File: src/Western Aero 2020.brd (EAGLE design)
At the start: 122.2 x 139.4 mm, 78 parts, among them IC1 7805DT, IC3 7806DT

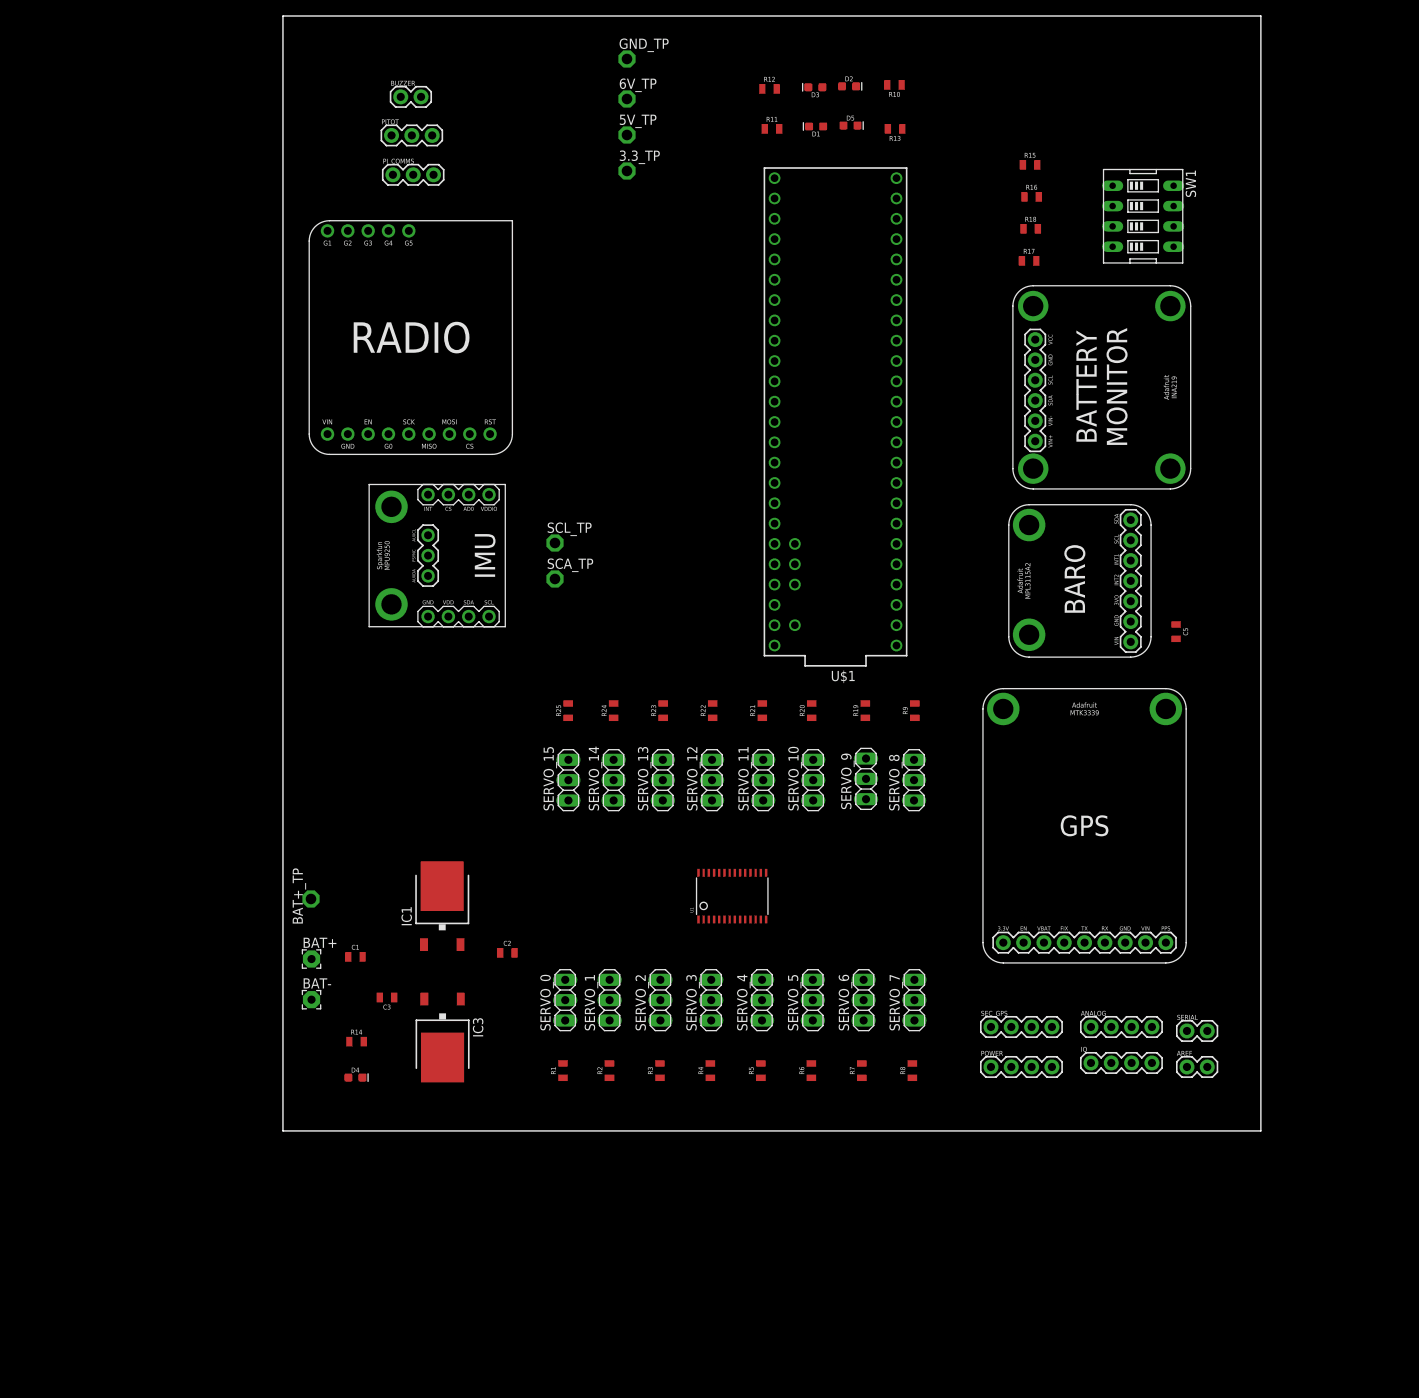
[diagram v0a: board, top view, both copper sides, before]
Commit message: Reconfigured components, hid resistors and cut space
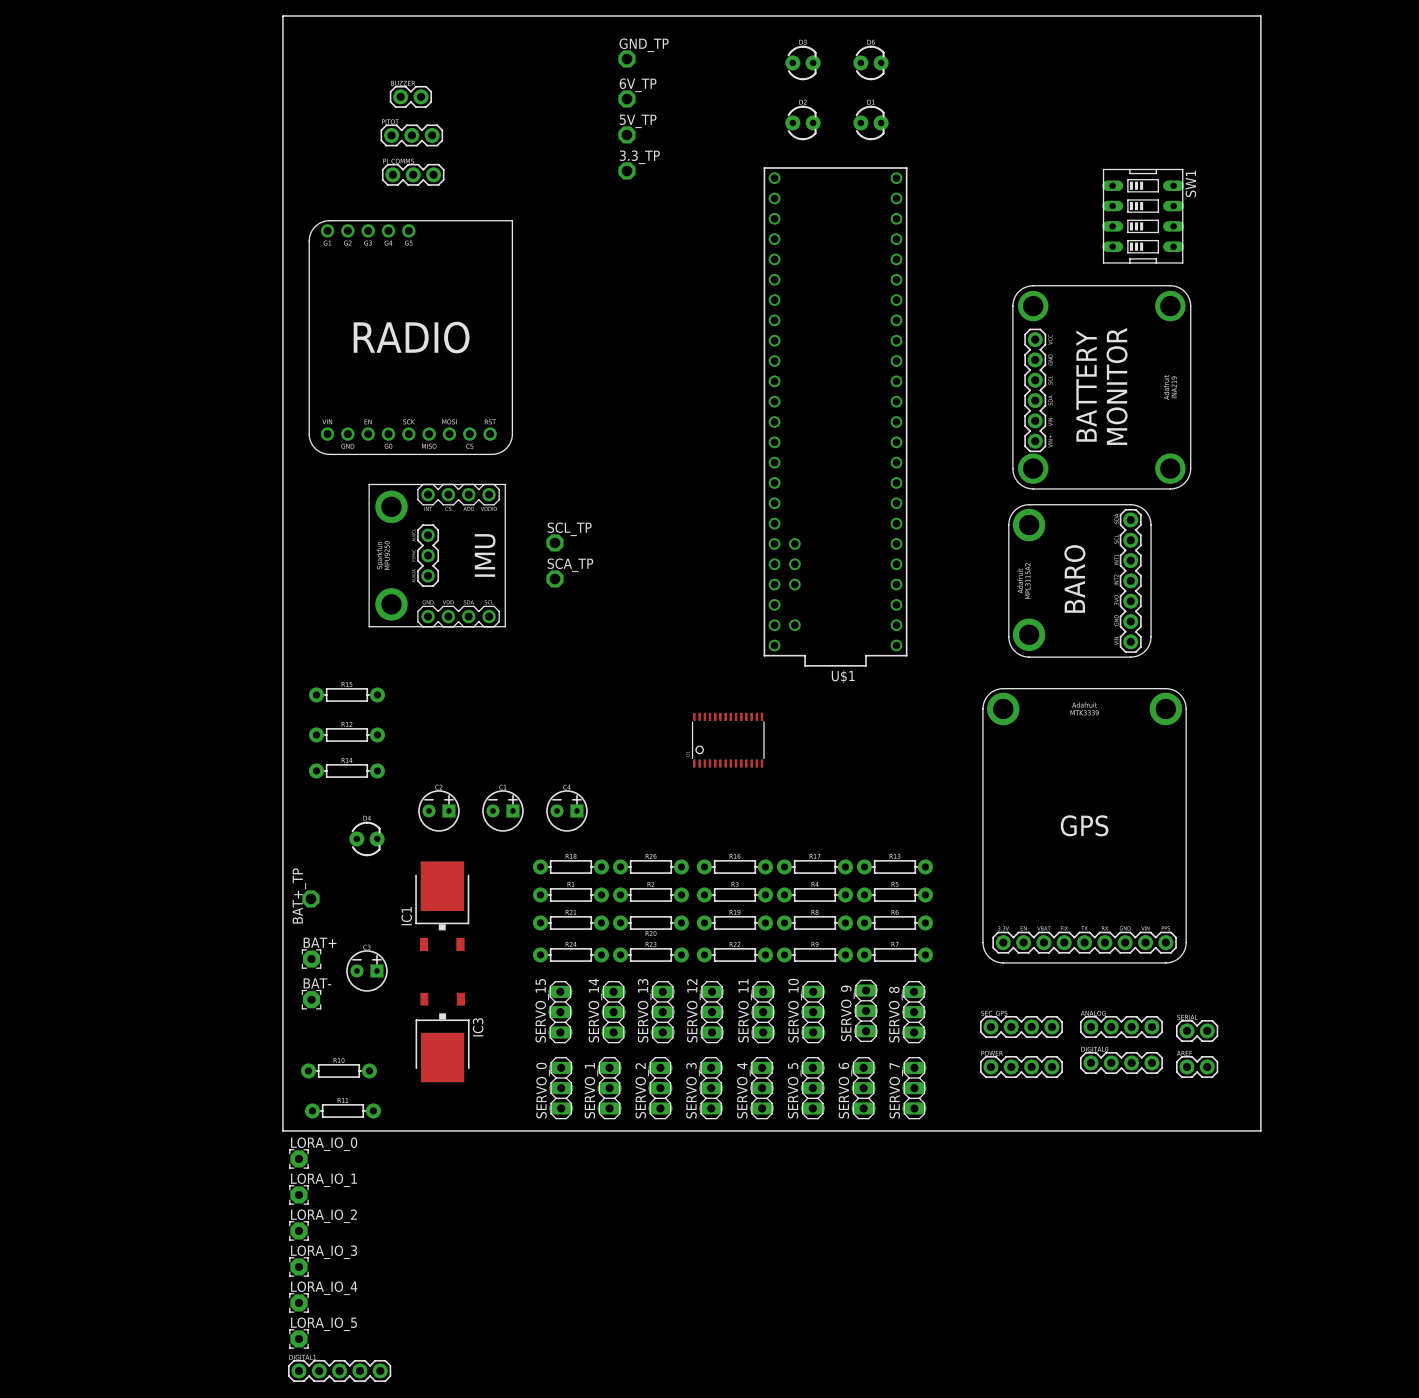
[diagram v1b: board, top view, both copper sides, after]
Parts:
- removed C5: 10µF, SparkFun-Capacitors:0805
- removed D5: WHITE, SparkFun-LED:LED-0603
- removed R25: 220, SparkFun-Resistors:0805
- added C4: 0.1uF, SparkFun-Capacitors:CPOL-RADIAL-2.5MM-5MM
- added D6: Red, SparkFun-LED:LED_3MM
- added DIGITAL1: (no value), SparkFun-Connectors:1X05
- added LORA_IO_0, LORA_IO_1, LORA_IO_2, LORA_IO_3, LORA_IO_4, LORA_IO_5: WIREPAD, wirepad:2,15/1,0
- added R26: 10K, SparkFun-Resistors:AXIAL-0.3
- C1: value 0.33µF -> 10uF; device SparkFun-Capacitors:0805 -> SparkFun-Capacitors:CPOL-RADIAL-2.5MM-5MM
- C2: value 0.1µF -> 0.1uF; device SparkFun-Capacitors:0805 -> SparkFun-Capacitors:CPOL-RADIAL-2.5MM-5MM
- C3: value 0.1µF -> 0.33uF; device SparkFun-Capacitors:0805 -> SparkFun-Capacitors:CPOL-RADIAL-2.5MM-5MM
- D1: value BLUE -> Blue; device SparkFun-LED:LED-0603 -> SparkFun-LED:LED_3MM
- D2: value RED -> Yellow; device SparkFun-LED:LED-0603 -> SparkFun-LED:LED_3MM
- D3: value Yellow -> White; device SparkFun-LED:LED-0603 -> SparkFun-LED:LED_3MM
- D4: value GREEN -> Green; device SparkFun-LED:LED-0603 -> SparkFun-LED:LED_3MM
- R1, R10, R11, R12, R13, R14, R15, R16, R17, R19, R2, R20, R21, R22, R23, R24, R3, R4, R5, R6, R7, R8, R9: device SparkFun-Resistors:0805 -> SparkFun-Resistors:AXIAL-0.3
- R18: value 10K -> 220; device SparkFun-Resistors:0805 -> SparkFun-Resistors:AXIAL-0.3
- moved R10 141.5 mm to (7.00, 7.50), turned to 0 degrees
- moved R11 134.0 mm to (7.50, 2.50)
- moved R15 108.1 mm to (8.00, 54.5)
- moved R18 98.3 mm to (36.0, 33.0)
- moved R12 96.5 mm to (8.00, 49.5)
- moved R13 92.3 mm to (76.5, 33.0), turned to 0 degrees
- moved R16 91.6 mm to (56.5, 33.0)
- moved R17 80.4 mm to (66.5, 33.0)
- moved R21 35.7 mm to (36.0, 26.0), turned to 0 degrees
- moved R14 33.9 mm to (8.00, 45.0)
- moved R20 33.3 mm to (46.0, 26.0), turned to 180 degrees
- moved R9 33.0 mm to (66.5, 22.0), turned to 0 degrees
- moved R19 31.1 mm to (56.5, 26.0), turned to 0 degrees
- moved R24 31.0 mm to (36.0, 22.0), turned to 0 degrees
- moved R22 30.7 mm to (56.5, 22.0), turned to 0 degrees
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- renumbered IO to DIGITAL0
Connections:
- removed net LORA_IO_1: U$1.35/A16, U$3.10
- removed net LORA_IO_2: U$1.36/A17, U$3.11
- removed net LORA_IO_3: U$1.37/A18, U$3.12
- removed net LORA_IO_4: U$1.38/A19, U$3.13
- removed net LORA_IO_5: U$1.39/A20, U$3.14
- new net D35: DIGITAL1.1, U$1.35/A16
- new net D36: DIGITAL1.2, U$1.36/A17
- new net D37: DIGITAL1.3, U$1.37/A18
- new net D38: DIGITAL1.4, U$1.38/A19
- new net D39: DIGITAL1.5, U$1.39/A20
- new net N$10: LORA_IO_2.1, U$3.11
- new net N$25: LORA_IO_4.1, U$3.13
- new net N$26: LORA_IO_3.1, U$3.12
- new net N$27: LORA_IO_0.1, U$3.4
- net 5V: now also C1.1, C4.1; no longer C2.1, C5.2
- net 6V: now also C2.1, SERVO_0.2; no longer C3.1
- net DIP1: now also R26.P$2; no longer R17.2
- net DIP2: now also R15.P$2; no longer R18.2
- net DIP3: now also R16.P$2; no longer R16.2
- net DIP4: now also R17.P$2; no longer R15.2
- net GND: now also C4.2, R10.P$1, R11.P$1, R12.P$1, R13.P$1, R14.P$1, R15.P$1, R16.P$1, R17.P$1, R26.P$1; no longer C5.1, R10.1, R11.1, R12.1, R13.1, R14.1, R15.1, R17.1
- net LORA_INT: no longer U$3.4
- net N$1: now also R18.P$2; no longer R1.2
- net N$11: now also R2.P$2; no longer R3.2
- net N$12: now also R3.P$2; no longer R4.2
- net N$13: now also R4.P$2; no longer R5.2
- net N$14: now also R5.P$2; no longer R6.2
- net N$15: now also R6.P$2; no longer R7.2
- net N$16: now also R7.P$2; no longer R8.2
- net N$17: now also R8.P$2; no longer R9.2
- net N$18: now also R9.P$2; no longer R19.2
- net N$19: now also R19.P$2; no longer R20.2
- net N$2: now also D6.K, R10.P$2; no longer R18.1
- net N$20: now also R20.P$2; no longer R21.2
- net N$21: now also R21.P$2; no longer R22.2
- net N$22: now also R22.P$2; no longer R23.2
- net N$23: now also R23.P$2; no longer R24.2
- net N$24: now also R24.P$2; no longer R25.2
- net N$3: now also D1.K, R11.P$2; no longer D2.C, R10.2
- net N$4: now also D2.K, R12.P$2; no longer R16.1
- net N$5: now also D3.K, R13.P$2; no longer D1.C, R11.2
- net N$6: now also D4.K, R14.P$2; no longer D3.C, R12.2
- net N$7: now also LORA_IO_5.1, U$3.14; no longer D5.C, R13.2
- net N$8: now also LORA_IO_1.1, U$3.10; no longer D4.C, R14.2
- net N$9: now also R1.P$2; no longer R2.2
- net PWM0: now also R18.P$1; no longer R1.1
- net PWM1: now also R1.P$1; no longer R2.1
- net PWM10: now also R19.P$1; no longer R20.1
- net PWM11: now also R20.P$1; no longer R21.1
- net PWM12: now also R21.P$1; no longer R22.1
- net PWM13: now also R22.P$1; no longer R23.1
- net PWM14: now also R23.P$1; no longer R24.1
- net PWM15: now also R24.P$1; no longer R25.1
- net PWM2: now also R2.P$1; no longer R3.1
- net PWM3: now also R3.P$1; no longer R4.1
- net PWM4: now also R4.P$1; no longer R5.1
- net PWM5: now also R5.P$1; no longer R6.1
- net PWM6: now also R6.P$1; no longer R7.1
- net PWM7: now also R7.P$1; no longer R8.1
- net PWM8: now also R8.P$1; no longer R9.1
- net PWM9: now also R9.P$1; no longer R19.1
- net RED_LED: now also D6.A; no longer D2.A
- net VIN-: now also C3.1; no longer C1.1
- net WHITE_LED: now also D3.A; no longer D5.A
- net YELLOW_LED: now also D2.A; no longer D3.A

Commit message: Added screwholes, adjusted addresses, few other tweaks
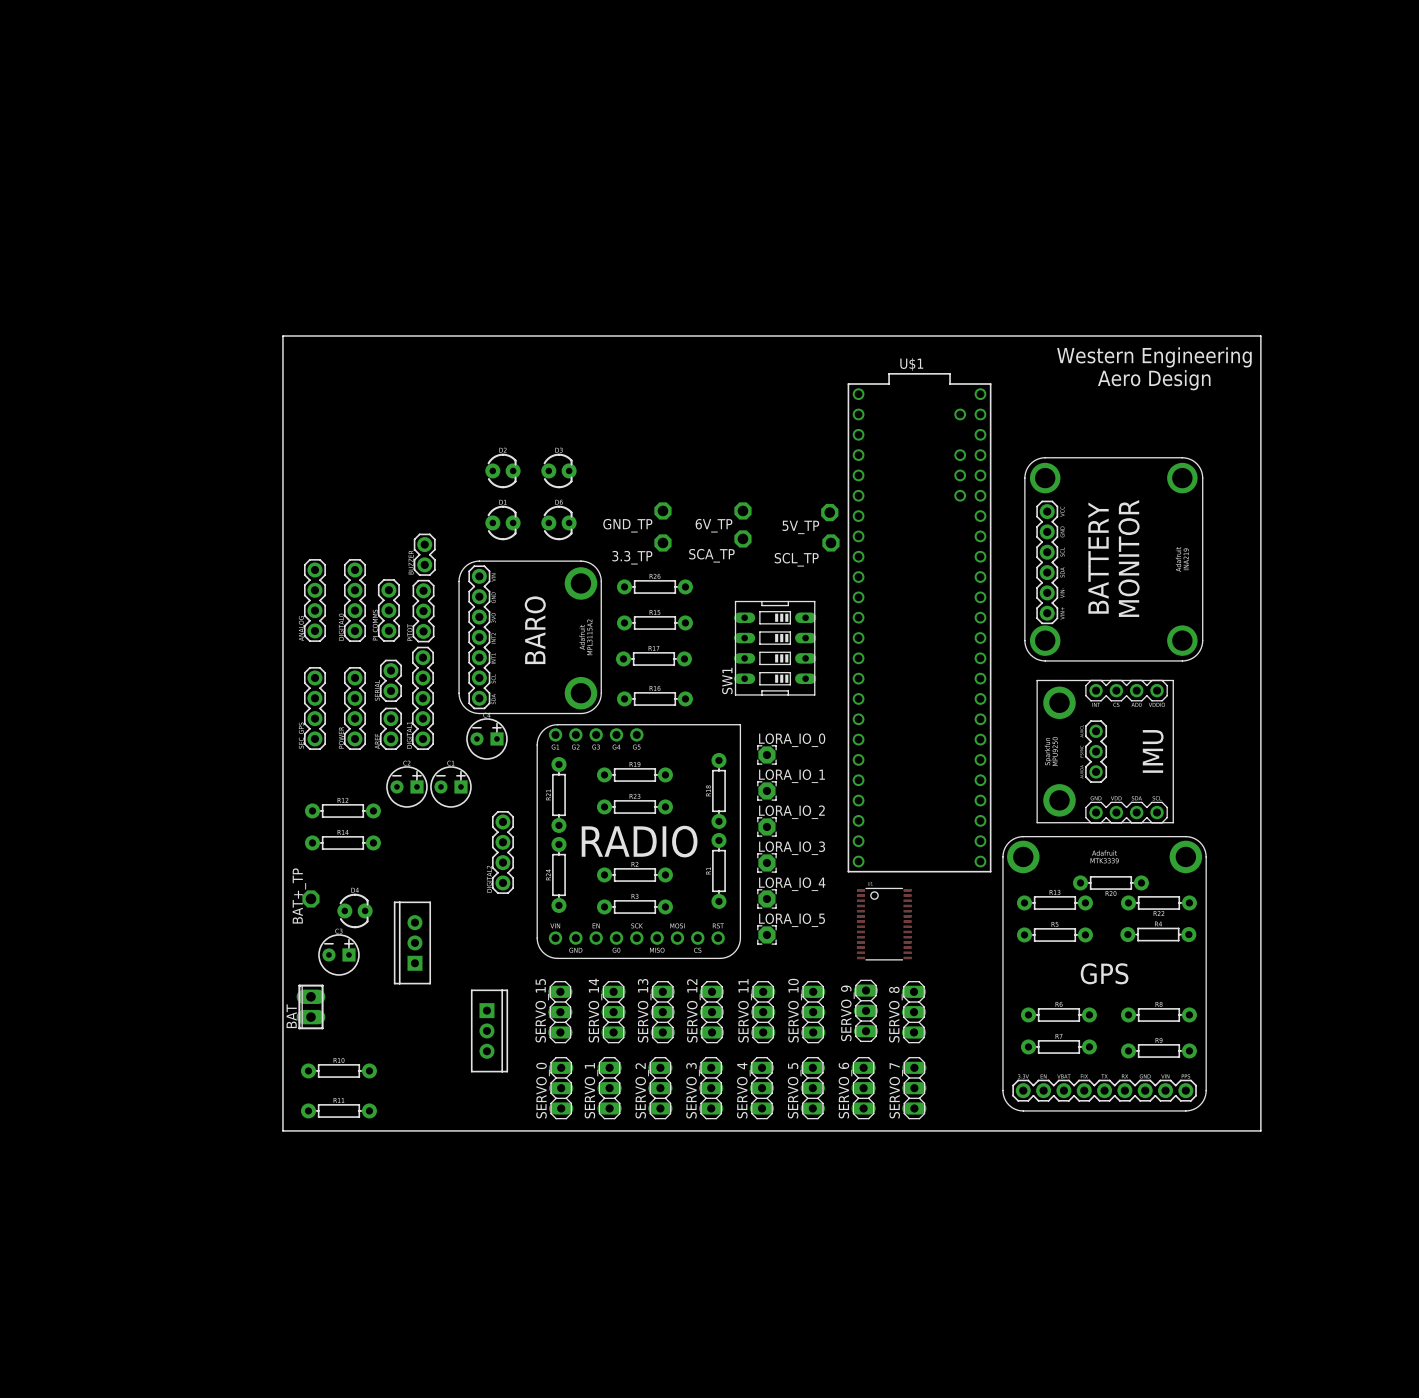
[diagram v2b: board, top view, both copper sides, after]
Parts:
- removed BAT+, BAT-: WIREPAD, wirepad:2,15/1,0
- removed IC1: 7805DT, linear:TO252
- removed IC3: 7806DT, linear:TO252
- added 7805, 7806: (no value), SparkFun-IC-Power:TO220-IGO
- added BAT: (no value), con-phoenix-254:2POL254
- added DIGITAL2: (no value), SparkFun-Connectors:1X04
- moved ANALOG 108.9 mm to (4.00, 62.5), turned to 90 degrees
- moved SERIAL 108.2 mm to (13.5, 55.0), turned to 90 degrees
- moved AREF 107.6 mm to (13.5, 49.0), turned to 90 degrees
- moved DIGITAL0 106.7 mm to (9.00, 62.5), turned to 90 degrees
- moved SEC_GPS 91.8 mm to (4.00, 49.0), turned to 90 degrees
- moved POWER 89.4 mm to (9.00, 49.0), turned to 90 degrees
- moved U$4 87.3 mm to (22.0, 71.2), turned to 270 degrees
- moved U$2 87.0 mm to (111.3, 56.3)
- moved DIGITAL1 80.5 mm to (17.5, 49.0), turned to 90 degrees
- moved LORA_IO_0 77.3 mm to (60.5, 47.0)
- moved LORA_IO_1 77.3 mm to (60.5, 42.5)
- moved LORA_IO_2 77.3 mm to (60.5, 38.0)
- moved LORA_IO_3 77.3 mm to (60.5, 33.5)
- moved LORA_IO_4 77.3 mm to (60.5, 29.0)
- moved LORA_IO_5 77.3 mm to (60.5, 24.5)
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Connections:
- removed net LORA_CS: U$1.33/A14, U$3.8
- new net CS: DIGITAL2.4, U$1.33/A14, U$3.8
- net 5V: now also 7805.OUT, U1.1, U1.2, U1.3; no longer IC1.2
- net 6V: now also 7806.OUT; no longer IC3.2
- net GND: now also 7805.GND, 7806.GND, BAT.1; no longer BAT-.1, IC1.3, IC3.3, U1.1, U1.2, U1.3
- net MISO: now also DIGITAL2.2
- net MOSI: now also DIGITAL2.3
- net SCK: now also DIGITAL2.1
- net VIN+: now also BAT.2; no longer BAT+.1
- net VIN-: now also 7805.IN, 7806.IN; no longer IC1.1, IC3.1
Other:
- board size 122.2 x 139.4 mm -> 122.2 x 99.4 mm
- board text added: "Western Engineering Aero Design"
